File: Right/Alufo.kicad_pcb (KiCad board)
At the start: 2 copper layers, 139.7 x 88.9 mm, 67 parts, among them J2 USB_C_Receptacle_USB2.0_16P_2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, J4 USB_C_Receptacle_USB2.0_16P_2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, K11 PG1350, K12 PG1350, K13 PG1350, K14 PG1350, K15 PG1350, K16 PG1350, K21 PG1350, K22 PG1350, K23 PG1350, K24 PG1350, K25 PG1350, K26 PG1350, K32 PG1350, K33 PG1350, K34 PG1350, K35 PG1350, K41 PG1350_1½U, K42 PG1350/SKQUCAA010, SW10 BOOT, U2 CH552T, U4 USBLC6-2P6, U6 USBLC6-2P6

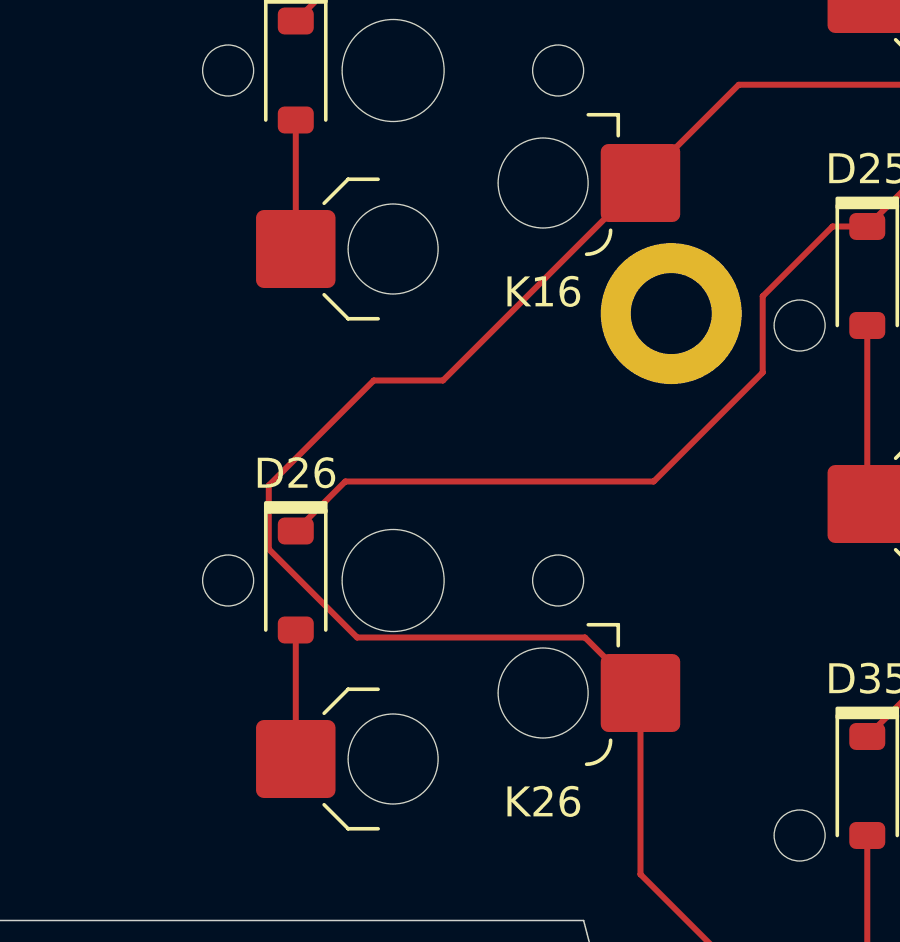
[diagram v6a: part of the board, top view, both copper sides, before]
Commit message: Tweak D26 location
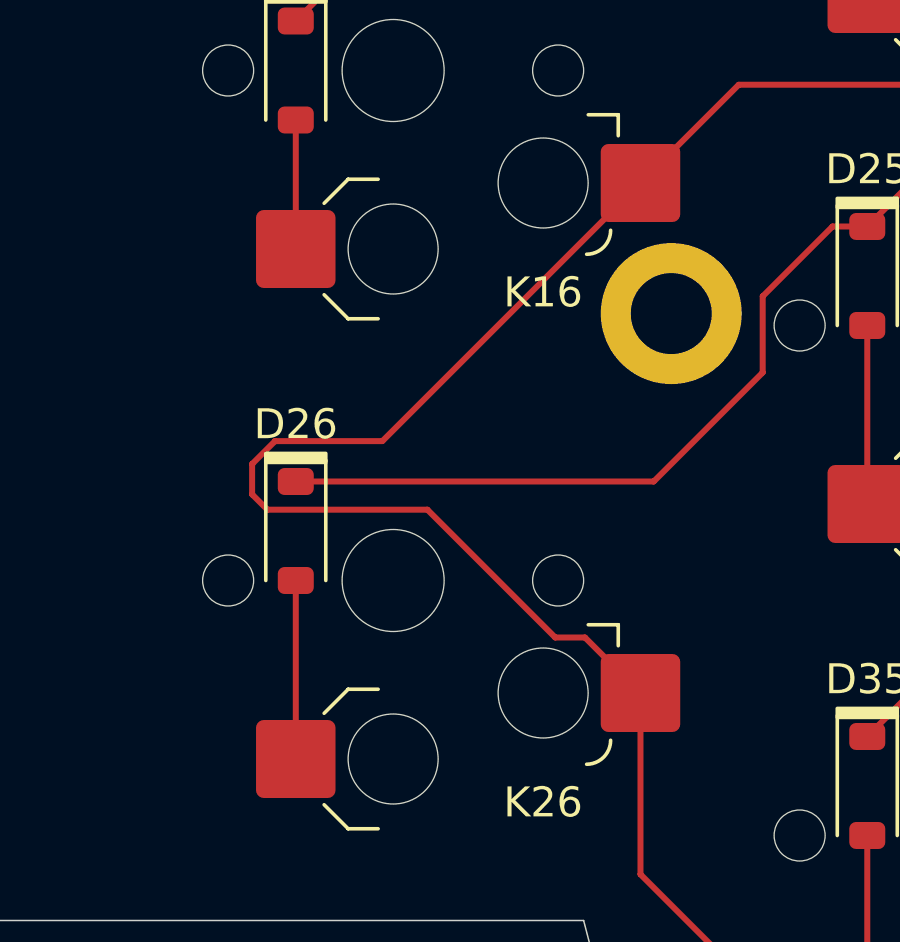
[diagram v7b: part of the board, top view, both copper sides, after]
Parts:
- moved D26 1.65 mm to (101.5, 67.8)
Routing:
- net Net-(D26-A): track 4.30 -> 5.95 mm
- net Row2: track 129.9 -> 129.2 mm
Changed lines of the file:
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@@
 	(footprint "Project Library:D_SOD-123_Mod"
 		(layer "F.Cu")
-		(at 101.53 69.416683 -90)
+		(at 101.53 67.766683 -90)
 		(descr "SOD-123")
 		(tags "SOD-123")
@@
 	)
 	(segment
-		(start 159.33 54.36668)
-		(end 166.305762 54.36668)
+		(start 113.461317 66.116683)
+		(end 117.094 62.484)
 		(width 0.2)
 		(layer "F.Cu")
@@
 	)
 	(segment
-		(start 119.421319 57.616681)
-		(end 120.58 57.616681)
+		(start 159.33 54.36668)
+		(end 166.305762 54.36668)
 		(width 0.2)
 		(layer "F.Cu")
@@
 	)
 	(segment
-		(start 103.18 66.116683)
-		(end 113.461317 66.116683)
-		(width 0.2)
-		(layer "F.Cu")
-		(net 7)
-	)
-	(segment
-		(start 117.094 59.944)
-		(end 119.421319 57.616681)
+		(start 167.057082 55.118)
+		(end 173.581319 55.118)
 		(width 0.2)
 		(layer "F.Cu")
@@
 	)
 	(segment
-		(start 167.057082 55.118)
-		(end 173.581319 55.118)
+		(start 173.581319 55.118)
+		(end 176.08 57.616681)
 		(width 0.2)
 		(layer "F.Cu")
@@
 	)
 	(segment
-		(start 173.581319 55.118)
-		(end 176.08 57.616681)
+		(start 119.421319 57.616681)
+		(end 120.58 57.616681)
 		(width 0.2)
 		(layer "F.Cu")
@@
 	)
 	(segment
+		(start 101.53 66.116683)
+		(end 113.461317 66.116683)
+		(width 0.2)
+		(layer "F.Cu")
+		(net 7)
+	)
+	(segment
 		(start 201.676 65.532)
 		(end 201.091317 66.116683)
@@
 	)
 	(segment
-		(start 117.094 62.484)
-		(end 117.094 59.944)
+		(start 120.58 57.616681)
+		(end 124.202681 53.994)
 		(width 0.2)
 		(layer "F.Cu")
@@
 	)
 	(segment
-		(start 120.58 57.616681)
-		(end 124.202681 53.994)
+		(start 117.094 62.484)
+		(end 117.094 59.944)
 		(width 0.2)
 		(layer "F.Cu")
@@
 	)
 	(segment
-		(start 101.53 67.766683)
-		(end 103.18 66.116683)
-		(width 0.2)
-		(layer "F.Cu")
-		(net 7)
-	)
-	(segment
-		(start 113.461317 66.116683)
-		(end 117.094 62.484)
+		(start 157.65732 53.994)
+		(end 158.68 55.01668)
 		(width 0.2)
 		(layer "F.Cu")
@@
 	)
 	(segment
-		(start 157.65732 53.994)
-		(end 158.68 55.01668)
+		(start 181.878681 55.118)
+		(end 191.539256 55.118)
 		(width 0.2)
 		(layer "F.Cu")
@@
 	)
 	(segment
-		(start 181.878681 55.118)
-		(end 191.539256 55.118)
+		(start 117.094 59.944)
+		(end 119.421319 57.616681)
 		(width 0.2)
 		(layer "F.Cu")
@@
 	)
 	(segment
+		(start 104.416679 64.77)
+		(end 100.838 64.77)
+		(width 0.2)
+		(layer "F.Cu")
+		(net 54)
+	)
+	(segment
 		(start 166.098768 53.594)
 		(end 149.802314 53.594)
@@
 	)
 	(segment
+		(start 100.584 67.056)
+		(end 105.918 67.056)
+		(width 0.2)
+		(layer "F.Cu")
+		(net 54)
+	)
+	(segment
 		(start 200.127678 99.604041)
 		(end 200.511495 99.220224)
@@
 	)
 	(segment
+		(start 100.076 66.548)
+		(end 100.584 67.056)
+		(width 0.2)
+		(layer "F.Cu")
+		(net 54)
+	)
+	(segment
 		(start 133.096 83.566)
 		(end 171.773314 83.566)
@@
 	)
 	(segment
-		(start 104.12866 62.74934)
-		(end 106.43734 62.74934)
+		(start 111.17 71.316683)
+		(end 113.02 73.166683)
 		(width 0.2)
 		(layer "F.Cu")
@@
 	)
 	(segment
-		(start 111.17 71.316683)
-		(end 103.574683 71.316683)
-		(width 0.2)
-		(layer "F.Cu")
-		(net 54)
-	)
-	(segment
 		(start 119.375836 85.566684)
 		(end 131.095316 85.566684)
@@
 	)
 	(segment
+		(start 105.918 67.056)
+		(end 110.178683 71.316683)
+		(width 0.2)
+		(layer "F.Cu")
+		(net 54)
+	)
+	(segment
 		(start 194.272 61.938)
 		(end 194.272 57.285058)
@@
 	)
 	(segment
+		(start 110.178683 71.316683)
+		(end 111.17 71.316683)
+		(width 0.2)
+		(layer "F.Cu")
+		(net 54)
+	)
+	(segment
 		(start 209.796786 63.855)
 		(end 208.519786 65.132)
@@
 	)
 	(segment
+		(start 100.838 64.77)
+		(end 100.076 65.532)
+		(width 0.2)
+		(layer "F.Cu")
+		(net 54)
+	)
+	(segment
 		(start 149.802314 53.594)
 		(end 148.587493 52.379179)
@@
 	)
 	(segment
-		(start 113.02 73.166683)
-		(end 111.17 71.316683)
-		(width 0.2)
-		(layer "F.Cu")
-		(net 54)
-	)
-	(segment
 		(start 211.733 63.855)
 		(end 209.796786 63.855)
@@
 	)
 	(segment
-		(start 106.43734 62.74934)
-		(end 113.02 56.166679)
+		(start 100.076 65.532)
+		(end 100.076 66.548)
 		(width 0.2)
 		(layer "F.Cu")
@@
 	)
 	(segment
-		(start 100.63 66.248)
-		(end 104.12866 62.74934)
-		(width 0.2)
-		(layer "F.Cu")
-		(net 54)
-	)
-	(segment
 		(start 177.946 96.158)
 		(end 180.232 96.158)
@@
 	)
 	(segment
-		(start 116.295 52.891679)
-		(end 113.02 56.166679)
-		(width 0.2)
-		(layer "F.Cu")
-		(net 54)
-	)
-	(segment
-		(start 100.63 68.372)
-		(end 100.63 66.248)
+		(start 113.02 56.166679)
+		(end 104.416679 64.77)
 		(width 0.2)
 		(layer "F.Cu")
@@
 	)
 	(segment
-		(start 103.574683 71.316683)
-		(end 100.63 68.372)
+		(start 116.295 52.891679)
+		(end 113.02 56.166679)
 		(width 0.2)
 		(layer "F.Cu")
@@
 	(segment
 		(start 101.53 75.366683)
-		(end 101.53 71.066683)
+		(end 101.53 69.416683)
 		(width 0.2)
 		(layer "F.Cu")

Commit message: Remove “L” and “R” from all labels
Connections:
- net RX_PR renamed RX_P
- net RX_R renamed RX
- net TX_PR renamed TX_P
- net TX_R renamed TX
- net USB_PR+ renamed USB_P+
- net USB_PR- renamed USB_P-
- net USB_R+ renamed USB+
- net USB_R- renamed USB-
- net VBUS_R renamed VBUS
- net VCC_R renamed VCC
